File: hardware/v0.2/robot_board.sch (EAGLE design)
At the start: 161 parts, among them J1 POWER_JACKPTH, Q1 DMP2035U, Q2 DMP2035U, Q3 DMP2035U-7, Q4 DMP2035U-7, U1 FT232RL-BASICSSOP, U10 DRV8839, U12 LM393, U16 LM393, U17 ATMEGA325PA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

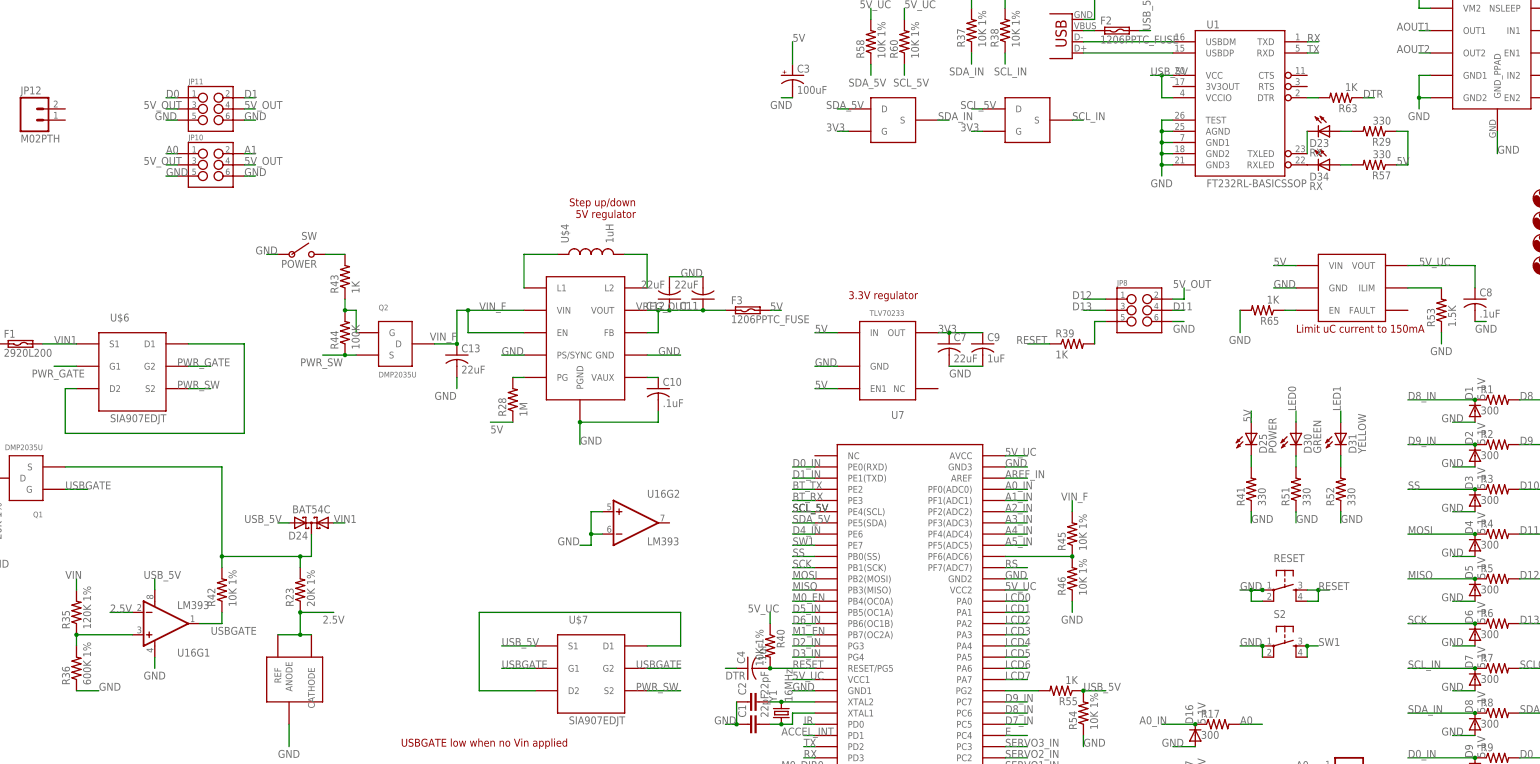
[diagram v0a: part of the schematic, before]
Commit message: fix servo code
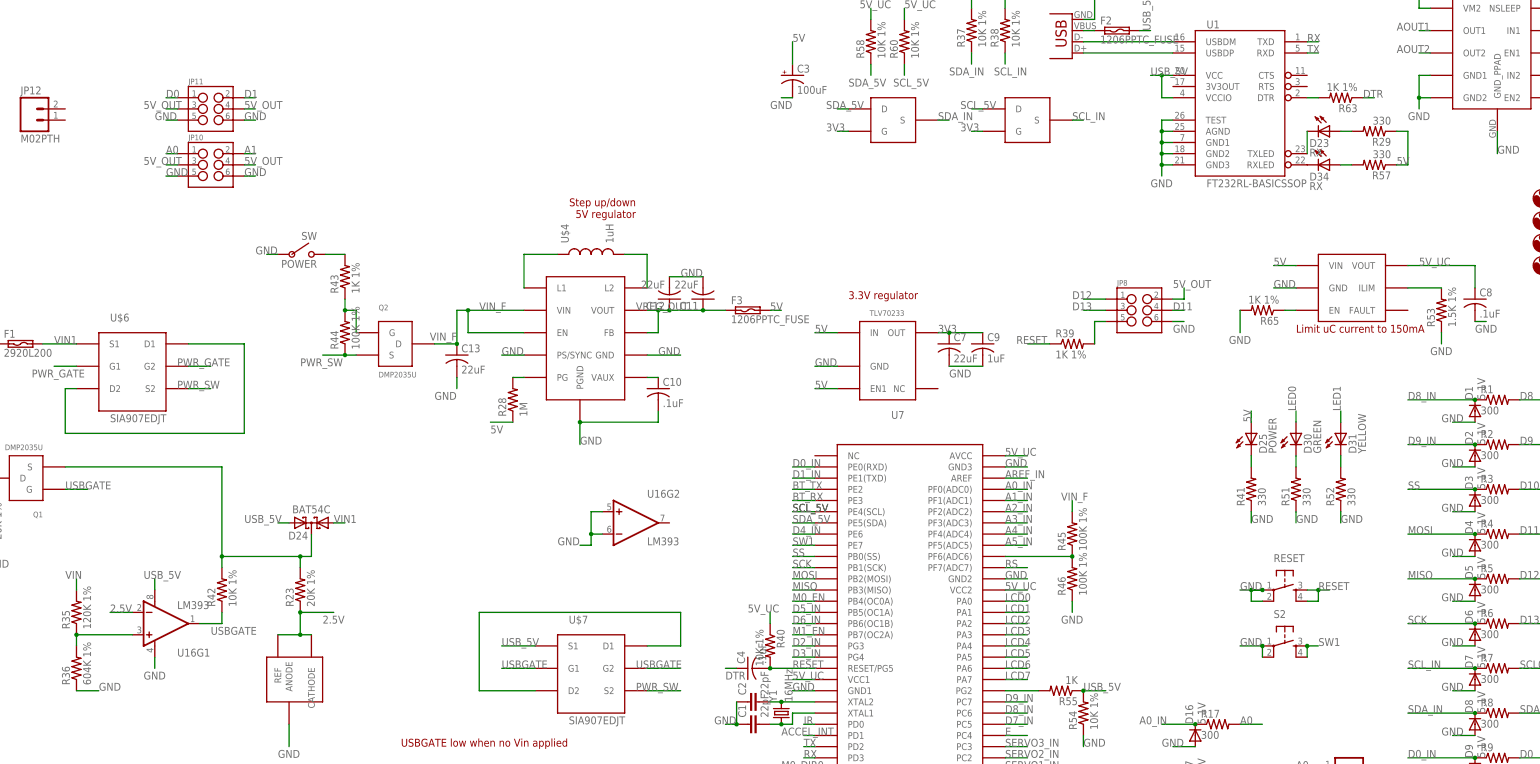
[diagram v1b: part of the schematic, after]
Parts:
- R36: value 600K 1% -> 604K 1%
- R39, R43, R63, R65: value 1K -> 1K 1%
- R44: value 100K -> 100K 1%
- R45, R46: value 10K 1% -> 100K 1%
- R53: value 1.5K -> 1.5K 1%
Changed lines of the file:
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@@
 <part name="U16" library="SparkFun-AnalogIC" deviceset="LM393" device=""/>
 <part name="R35" library="resistor" deviceset="R-US_" device="R1206" value="120K 1%"/>
-<part name="R36" library="resistor" deviceset="R-US_" device="R1206" value="600K 1%"/>
+<part name="R36" library="resistor" deviceset="R-US_" device="R1206" value="604K 1%"/>
 <part name="JP8" library="SparkFun-Connectors" deviceset="M03X2" device="2X3_SILK_SM"/>
-<part name="R39" library="resistor" deviceset="R-US_" device="R1206" value="1K"/>
+<part name="R39" library="resistor" deviceset="R-US_" device="R1206" value="1K 1%"/>
 <part name="R41" library="resistor" deviceset="R-US_" device="R1206" value="330"/>
 <part name="D25" library="SparkFun-LED" deviceset="LED-GREEN" device="LILYPAD" value="POWER"/>
@@
 <part name="Q2" library="jseng" deviceset="DMP2035U" device=""/>
 <part name="POWER" library="r_cubed" deviceset="SW" device=""/>
-<part name="R43" library="resistor" deviceset="R-US_" device="R1206" value="1K"/>
-<part name="R44" library="resistor" deviceset="R-US_" device="R1206" value="100K"/>
+<part name="R43" library="resistor" deviceset="R-US_" device="R1206" value="1K 1%"/>
+<part name="R44" library="resistor" deviceset="R-US_" device="R1206" value="100K 1%"/>
 <part name="U$19" library="r_cubed" deviceset="2POS_TERMINAL" device=""/>
 <part name="U$20" library="r_cubed" deviceset="2POS_TERMINAL" device=""/>
-<part name="R45" library="resistor" deviceset="R-US_" device="R1206" value="10K 1%"/>
-<part name="R46" library="resistor" deviceset="R-US_" device="R1206" value="10K 1%"/>
+<part name="R45" library="resistor" deviceset="R-US_" device="R1206" value="100K 1%"/>
+<part name="R46" library="resistor" deviceset="R-US_" device="R1206" value="100K 1%"/>
 <part name="U1" library="SparkFun-DigitalIC" deviceset="FT232RL-BASIC" device="SSOP"/>
 <part name="R47" library="resistor" deviceset="R-US_" device="R1206" value="300"/>
@@
 <part name="R52" library="resistor" deviceset="R-US_" device="R1206" value="330"/>
 <part name="U8" library="jseng" deviceset="MIC2009A" device=""/>
-<part name="R53" library="resistor" deviceset="R-US_" device="R1206" value="1.5K"/>
+<part name="R53" library="resistor" deviceset="R-US_" device="R1206" value="1.5K 1%"/>
 <part name="R54" library="resistor" deviceset="R-US_" device="R1206" value="10K 1%"/>
 <part name="R55" library="resistor" deviceset="R-US_" device="R1206" value="1K"/>
@@
 <part name="C8" library="resistor" deviceset="C-US" device="C1206" value=".1uF"/>
 <part name="C9" library="resistor" deviceset="C-US" device="C1206" value="1uF"/>
-<part name="R63" library="resistor" deviceset="R-US_" device="R1206" value="1K"/>
+<part name="R63" library="resistor" deviceset="R-US_" device="R1206" value="1K 1%"/>
 <part name="U$2" library="r_cubed" deviceset="POT" device=""/>
 <part name="D34" library="SparkFun-LED" deviceset="LED-GREEN" device="LILYPAD" value="RX"/>
-<part name="R65" library="resistor" deviceset="R-US_" device="R1206" value="1K"/>
+<part name="R65" library="resistor" deviceset="R-US_" device="R1206" value="1K 1%"/>
 <part name="D24" library="diode" deviceset="BAT54C" device=""/>
 <part name="R28" library="resistor" deviceset="R-US_" device="R1206" value="1M"/>
